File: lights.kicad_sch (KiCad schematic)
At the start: 29 parts, among them Q1 2N7002, Q2 2N7002, Q3 2N7002, Q4 2N7002, Q5 2N7002, U2 SI8261ABC-IS, U3 SI8261ABC-IS, U4 SI8261ABC-IS, U5 SI8261ABC-IS, U6 SI8261ABC-IS

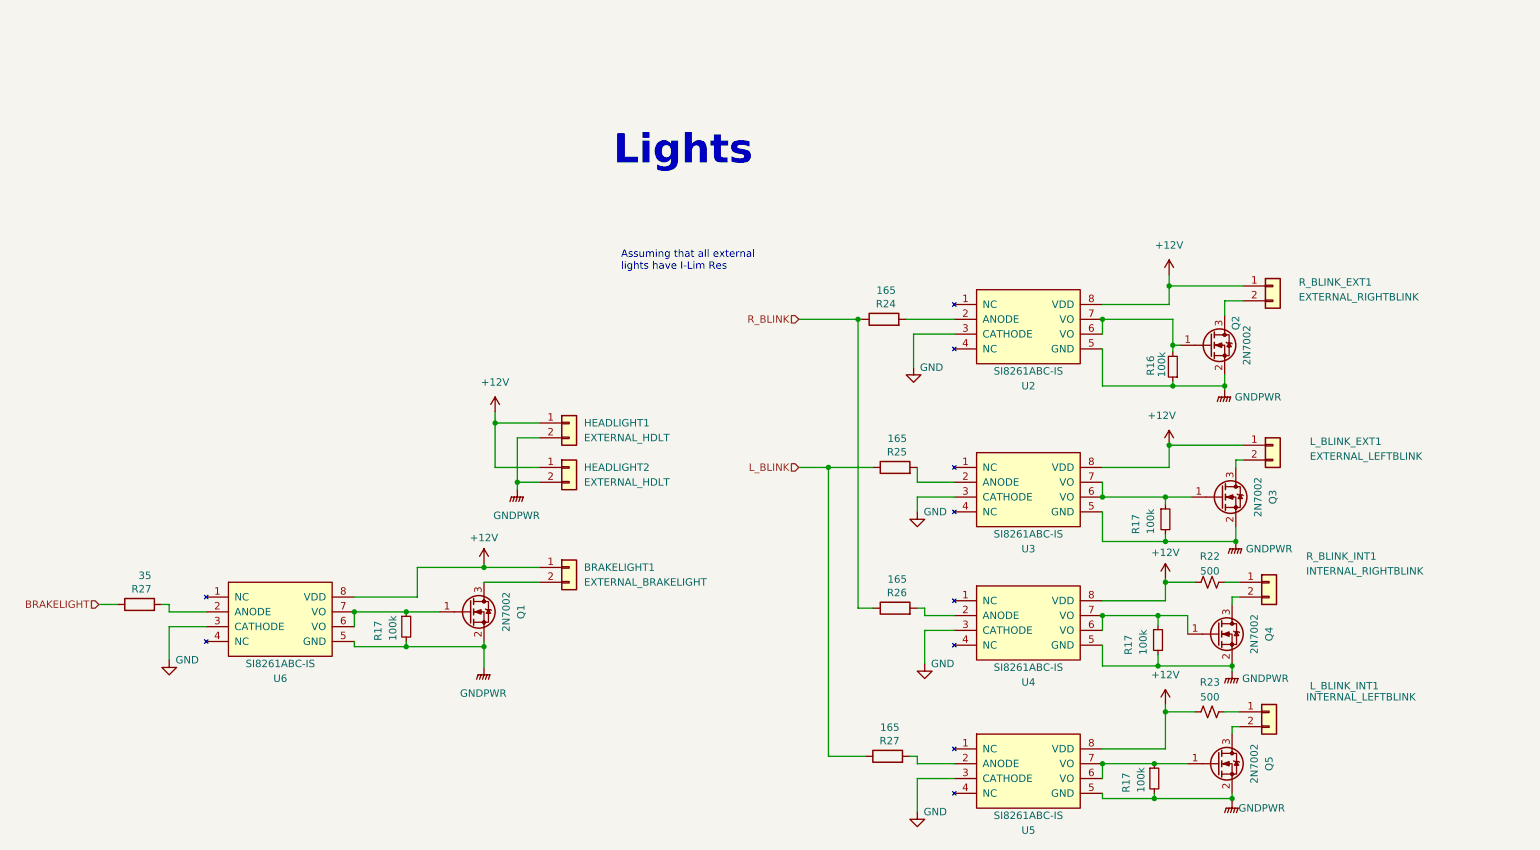
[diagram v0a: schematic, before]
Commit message: changed resistor values, updated footprints
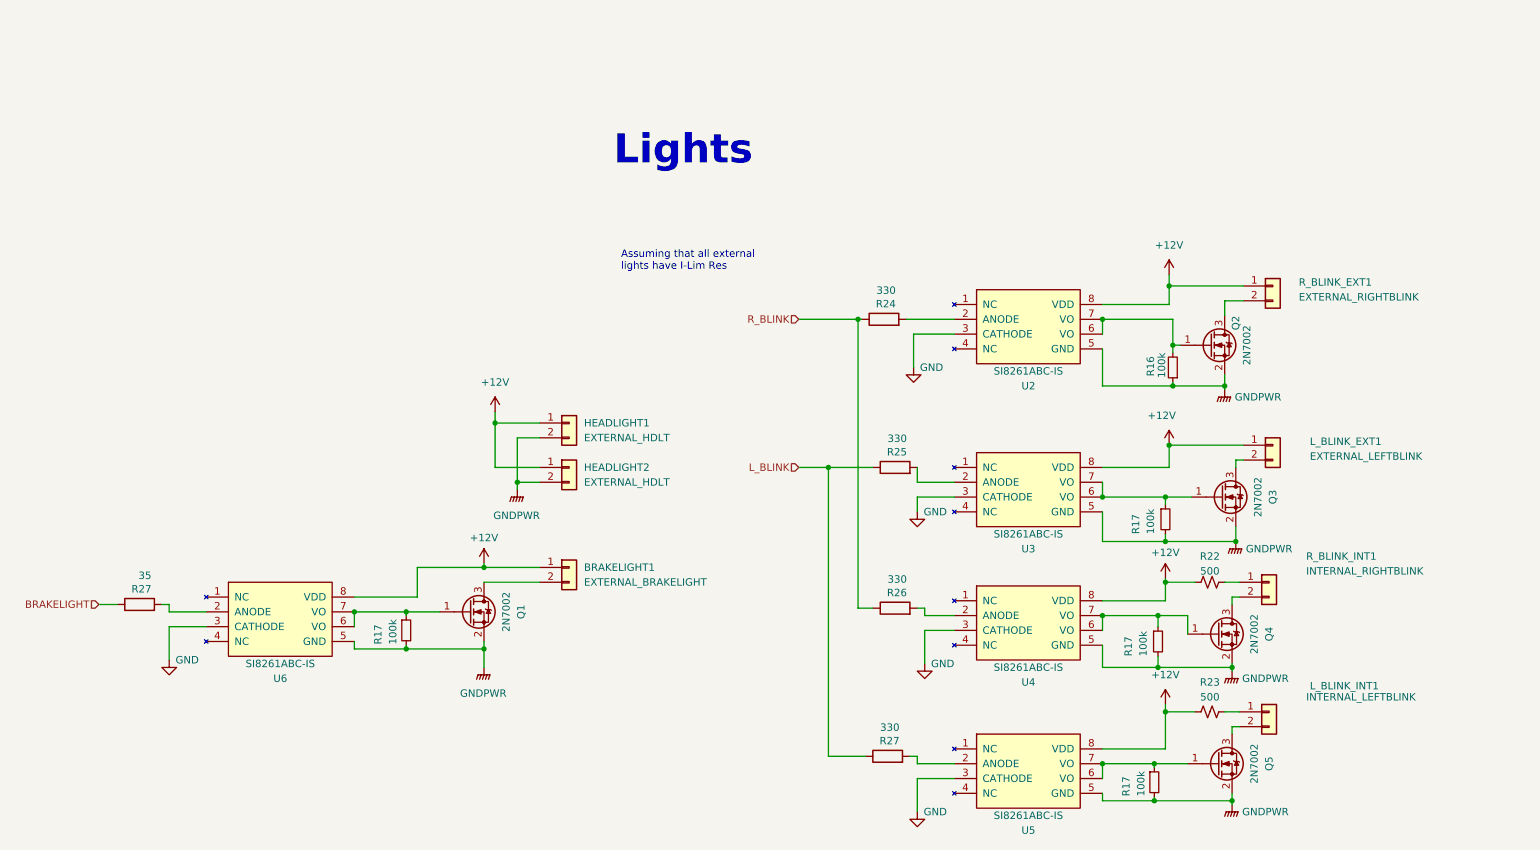
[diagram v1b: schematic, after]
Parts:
- R24, R25, R26, R27: value 165 -> 330
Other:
- moved on the sheet: R17

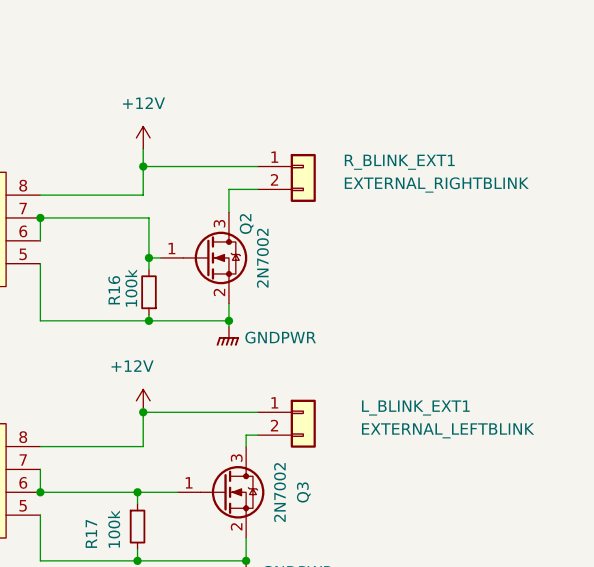
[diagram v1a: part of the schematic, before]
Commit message: Added drived fan circuitry
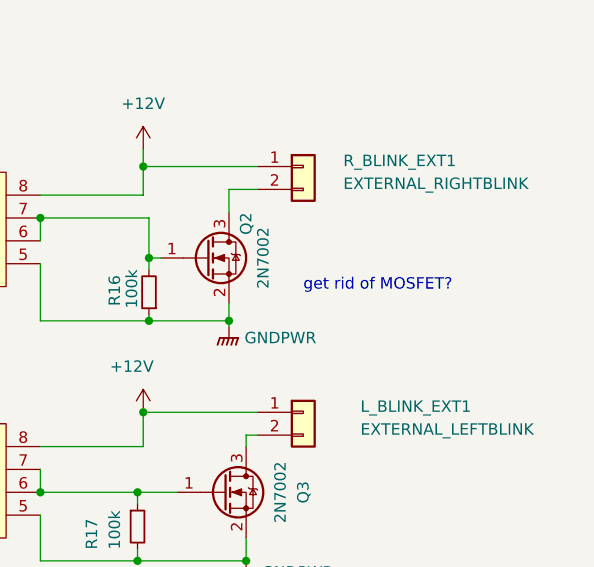
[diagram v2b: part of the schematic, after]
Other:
- note added: "get rid of MOSFET?"
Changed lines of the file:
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@@
     (stroke (width 0) (type default))
+  )
+  (text "get rid of MOSFET?\n" (at 237.49 74.93 0)
+    (effects (font (size 1.27 1.27)) (justify left bottom))
   )
   (text "Assuming that all external \nlights have I-Lim Res" (at 125.73 58.42 0)

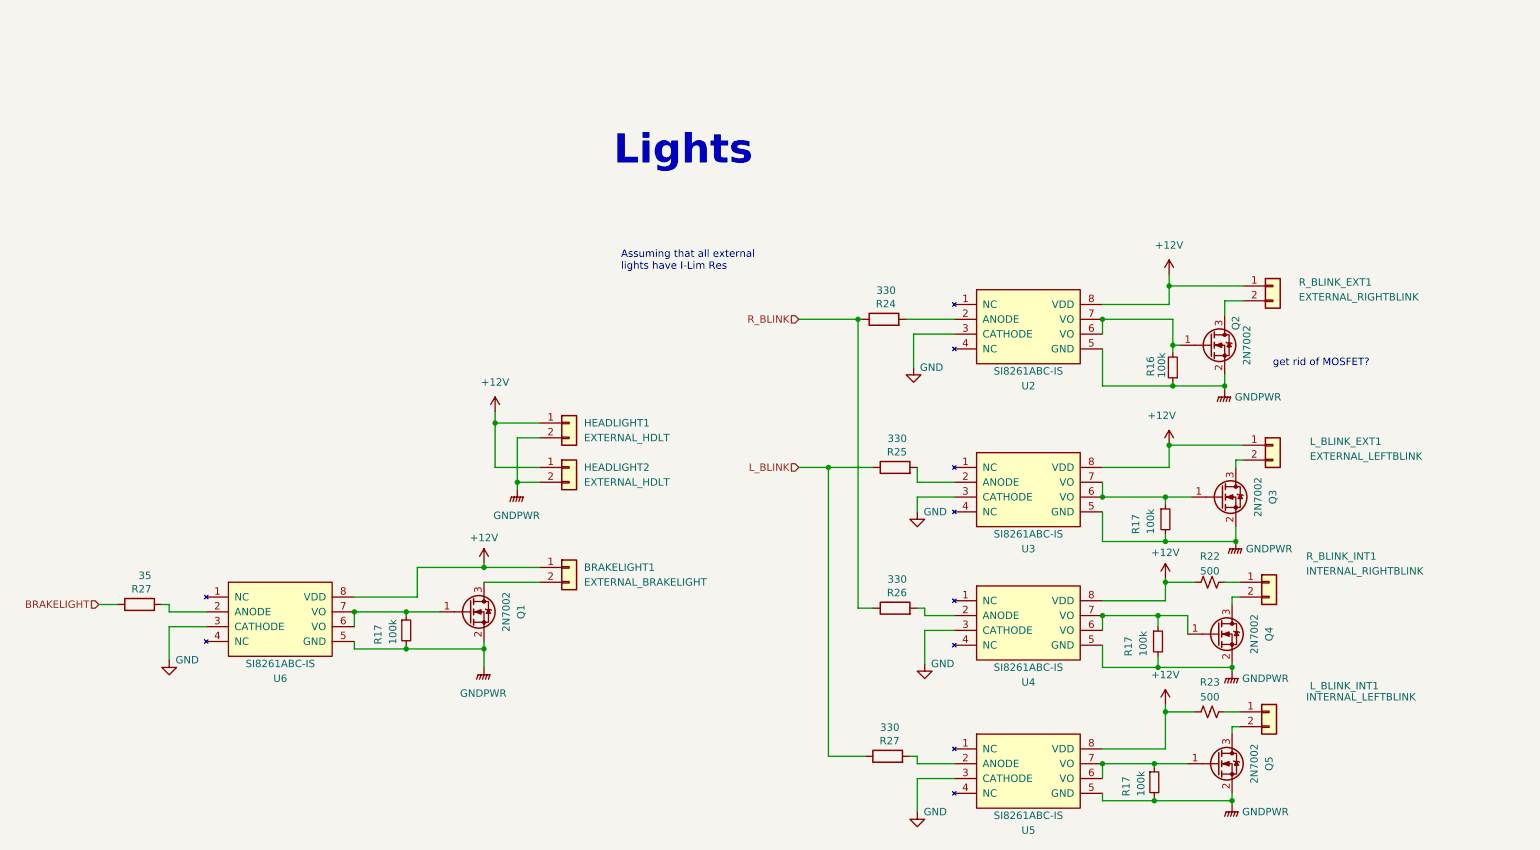
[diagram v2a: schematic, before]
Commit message: Added resistor to fan isolator, fixed ERC errors and warnings
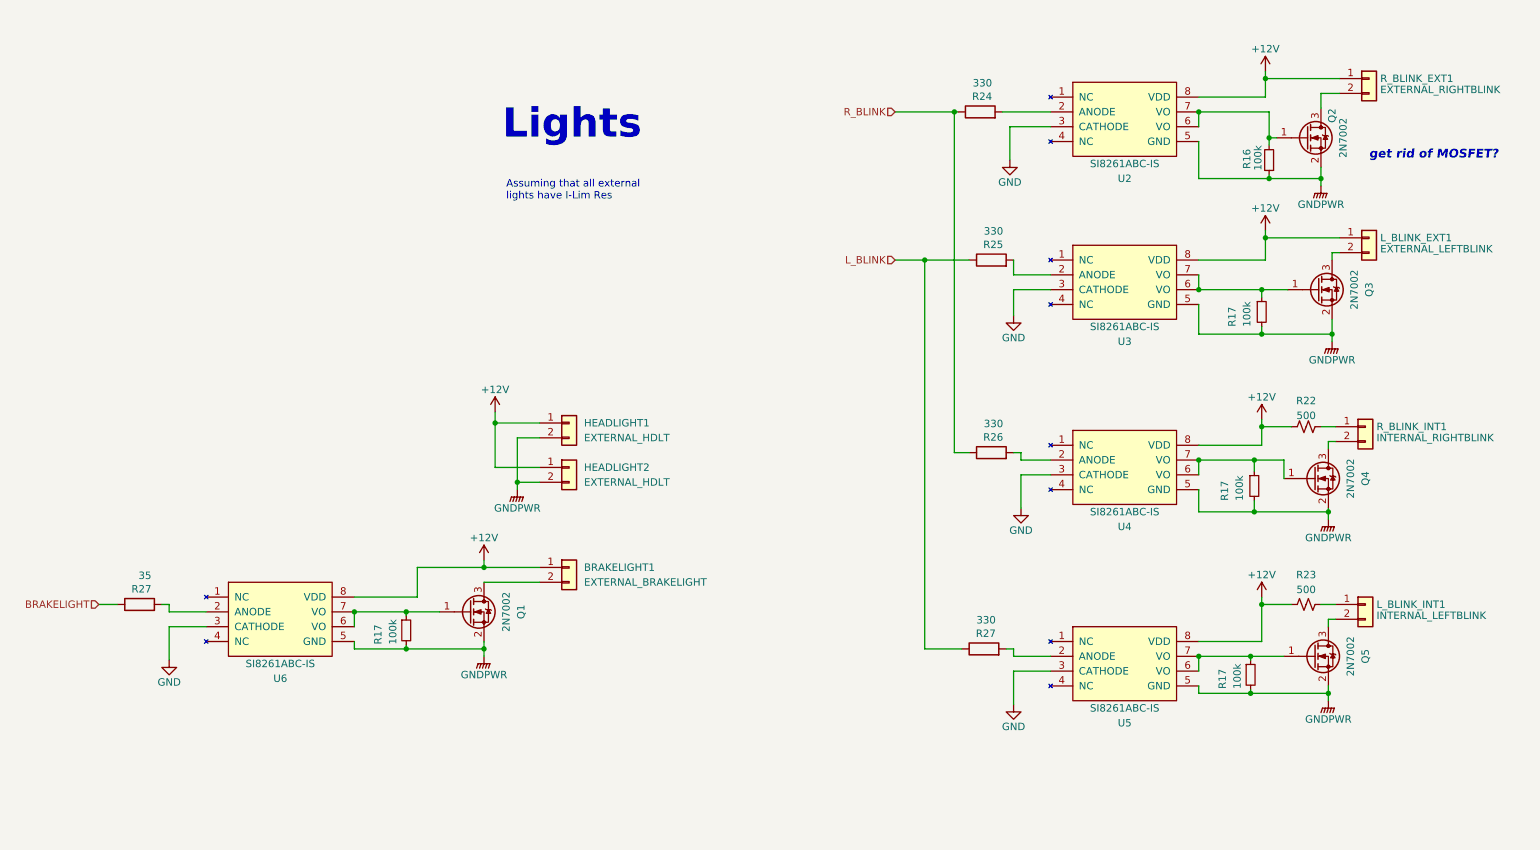
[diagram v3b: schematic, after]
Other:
- moved on the sheet: L_BLINK_EXT1, L_BLINK_INT1, Q2, Q3, Q4, Q5, R16, R17, R22, R23, R24, R25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

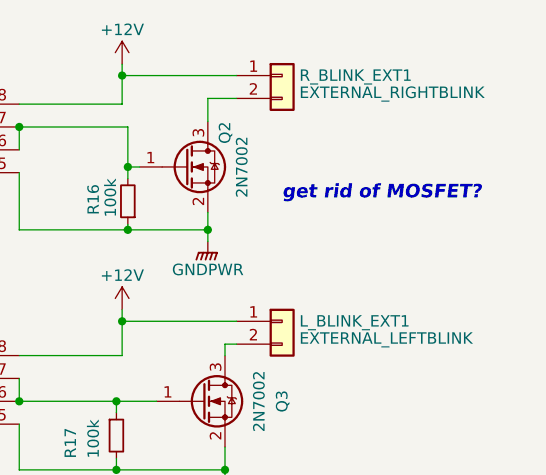
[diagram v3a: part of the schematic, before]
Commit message: changed labels for some connectors
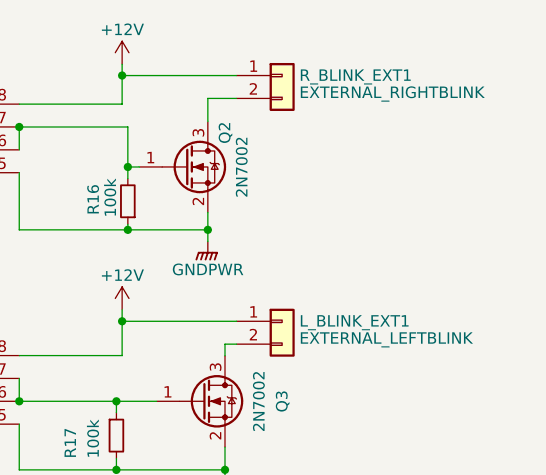
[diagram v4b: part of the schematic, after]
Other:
- note removed: "get rid of MOSFET?"
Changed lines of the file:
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@@
     (stroke (width 0) (type default))
-  )
-  (text "get rid of MOSFET?\n" (at 254 39.37 0)
-    (effects (font (size 1.5 1.5) (thickness 0.3) bold italic) (justify left bottom))
   )
   (text "Assuming that all external \nlights have I-Lim Res" (at 106.045 46.355 0)

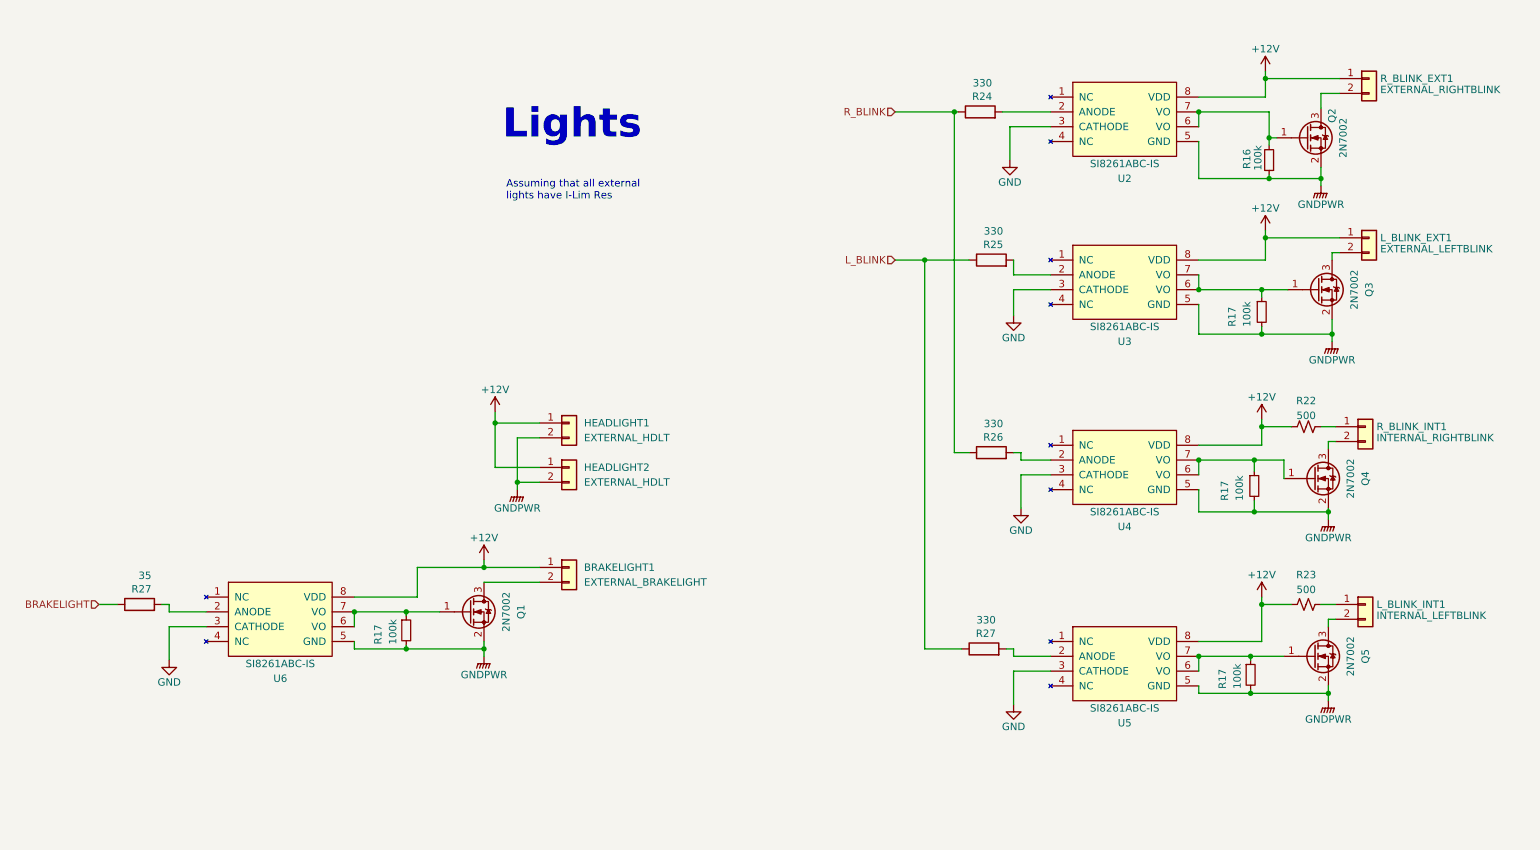
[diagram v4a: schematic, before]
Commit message: lower power optocouplers now used for lights and fans, updated version history
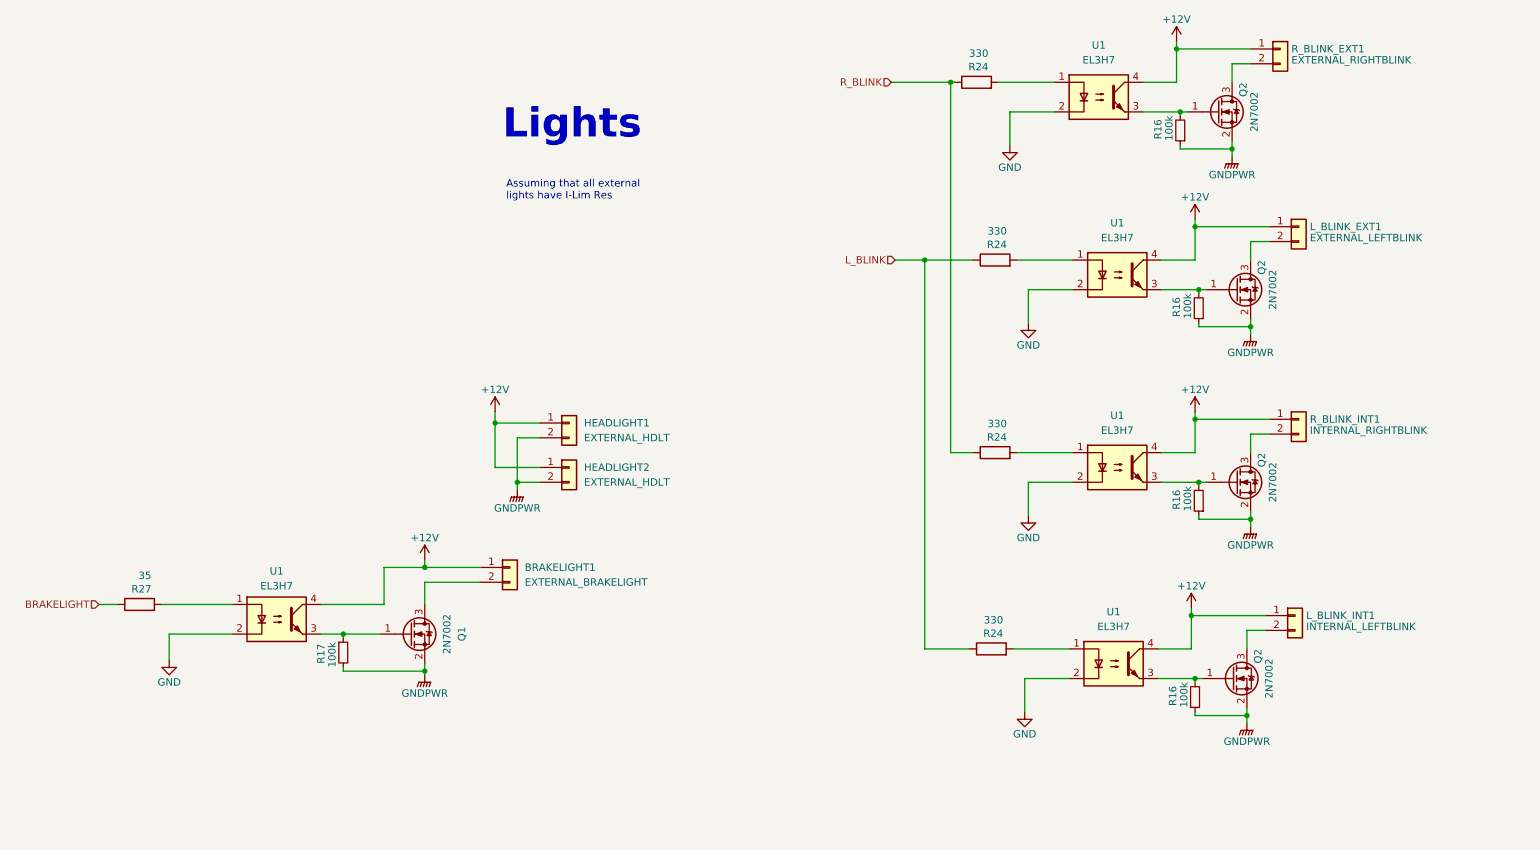
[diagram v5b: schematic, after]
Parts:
- removed Q3, Q4, Q5: 2N7002, Package_TO_SOT_SMD:SOT-23, symbol Transistor_FET:2N7002
- removed R17 (x3): 100k, Resistor_SMD:R_0805_2012Metric, symbol Device:R_Small
- removed R22, R23: 500, Resistor_SMD:R_0805_2012Metric, symbol Device:R_Small_US
- removed R25, R26, R27: 330, Resistor_SMD:R_0805_2012Metric, symbol Device:R
- removed U2, U3, U4, U5, U6: SI8261ABC-IS, Package_SO:SOIC-8_3.9x4.9mm_P1.27mm, symbol utsvt-bps:SI8261ABC-IS
- added Q2 (x3): 2N7002, Package_TO_SOT_SMD:SOT-23, symbol Transistor_FET:2N7002
- added R16 (x3): 100k, Resistor_SMD:R_0805_2012Metric, symbol Device:R_Small
- added R24 (x3): 330, Resistor_SMD:R_0805_2012Metric, symbol Device:R
- added U1 (x5): EL3H7, Package_SO:SOP-4_4.4x2.6mm_P1.27mm, symbol Isolator:EL817
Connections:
- net +12V: now also L_BLINK_INT1.1 (Pin_1), R_BLINK_INT1.1 (Pin_1), U1.4, U1.4, U1.4, U1.4, U1.4
- net GND: now also U1.2, U1.2, U1.2, U1.2, U1.2
- net GNDPWR: now also Q2.2 (S), Q2.2 (S), Q2.2 (S), R16.1, R16.1, R16.1
- net L_BLINK: now also R24.1, R24.1
- net R_BLINK: now also R24.1
- net at R27.2: now also U1.1
- net at Q1.1 (G), R17.1: now also U1.3
- net at Q2.1 (G), R16.2: now also U1.3
- net at R_BLINK_INT1.2 (Pin_2): now also Q2.3 (D)
- net at L_BLINK_INT1.2 (Pin_2): now also Q2.3 (D)
- net at L_BLINK_EXT1.2 (Pin_2): now also Q2.3 (D)
- net at R24.2: now also U1.1
- new net: Q2.1 (G), R16.2, U1.3 (x3)
- new net: R24.2, U1.1 (x3)
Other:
- moved on the sheet: BRAKELIGHT1, L_BLINK_EXT1, L_BLINK_INT1, Q1, Q2, R16, R17, R24, R_BLINK_EXT1, R_BLINK_INT1

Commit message: updated footprints and part numbers, added motor CAN 12V connection
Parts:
- BRAKELIGHT1, R_BLINK_EXT1, R_BLINK_INT1: Mauser PN (none) -> 538-43650-0215; P/N 43650-0215 -> (none); PN (none) -> 43650-0215
- HEADLIGHT1, HEADLIGHT2, L_BLINK_EXT1, L_BLINK_INT1: P/N 43650-0215 -> (none); PN (none) -> 43650-0215
- Q1, Q2: Mauser PN (none) -> 771-2N7002HR; P/N 2N7002HR -> (none); PN (none) -> 2N7002HR
- R16, R17: Mauser PN (none) -> 71-CRCW0805100KFKEAC; P/N CRCW0805100KFKEAC -> (none); PN (none) -> CRCW0805100KFKEAC
- R24: Mauser PN (none) -> 71-CRCW0805330RJNEAH; P/N SDR10EZPJ152 -> (none); PN (none) -> CRCW0805330RJNEAHP
- R27: Mauser PN (none) -> 791-WR08X35R2FTL; P/N SDR10EZPJ152 -> (none); PN (none) -> WR08X35R2FTL
- U1: Mauser PN (none) -> 638-EL3H7DTAVG; Mouser Part Number 638-EL3H7DTAVG -> (none); PN (none) -> EL3H7(D)(TA)-VG
